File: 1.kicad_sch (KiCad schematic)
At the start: 7 parts, among them Q1 BC107, Q2 BC107, Q3 BC107, Q4 BC107

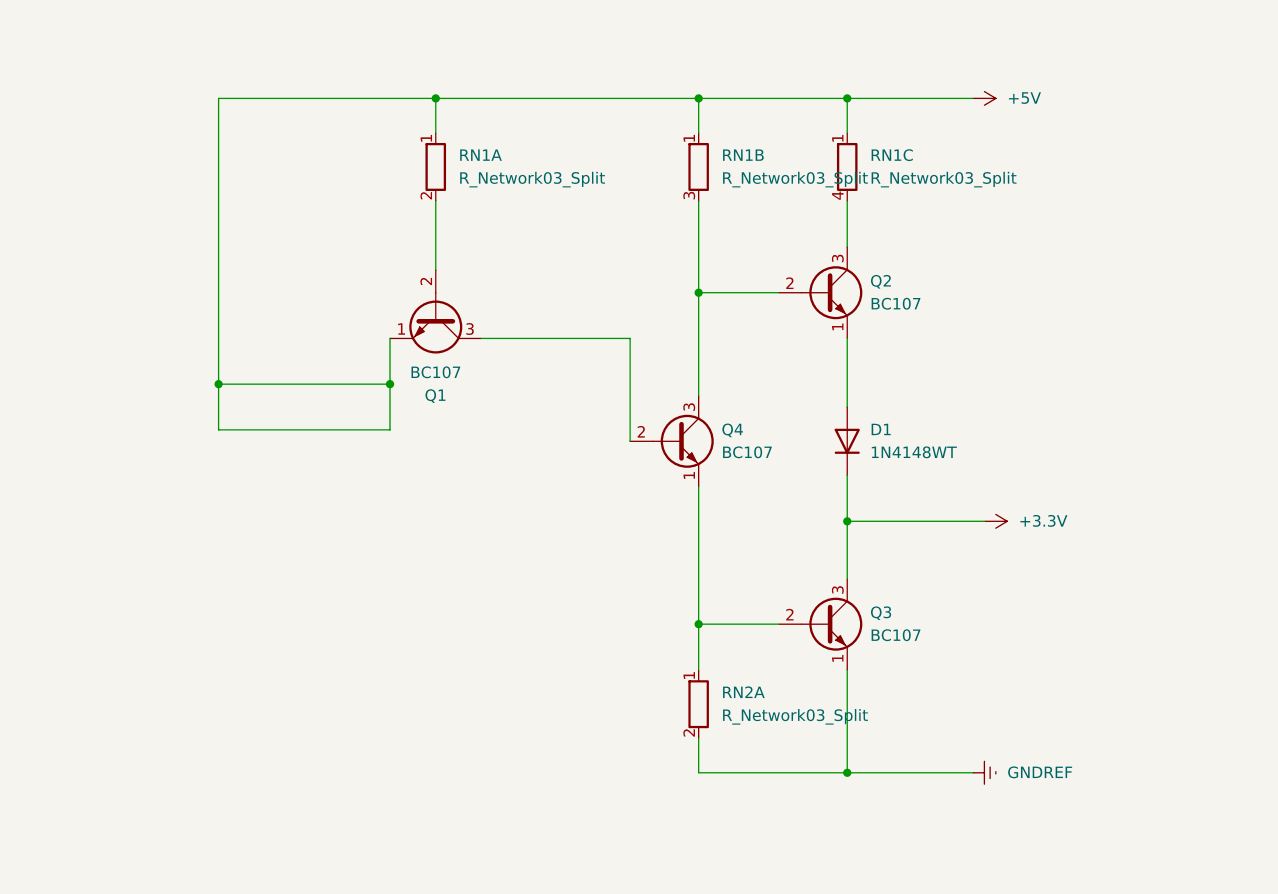
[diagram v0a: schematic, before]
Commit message: 1-create_basic_NAND_logic_discrete_gate: Create correct basic NAND gate schematic.
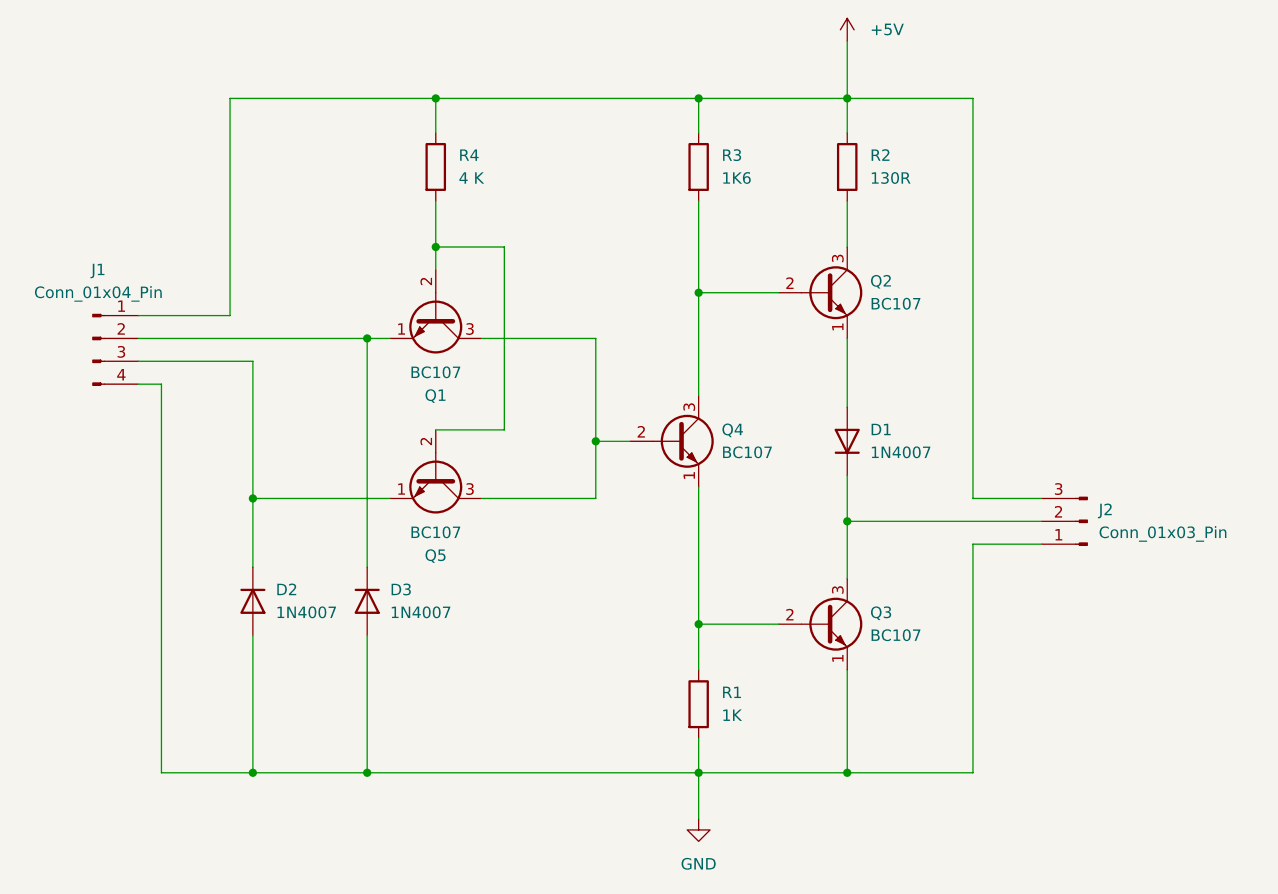
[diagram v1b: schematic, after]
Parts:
- removed D1: 1N4148WT, Diode_SMD:D_SOD-523, symbol Diode:1N4148WT
- removed RN1, RN2: R_Network03_Split, Resistor_THT:R_Array_SIP4, symbol Device:R_Network03_Split
- added D1, D2, D3: 1N4007, Diode_THT:D_DO-41_SOD81_P10.16mm_Horizontal, symbol Diode:1N4007
- added J1: Conn_01x04_Pin, Connector_PinHeader_2.54mm:PinHeader_1x04_P2.54mm_Vertical, symbol Connector:Conn_01x04_Pin
- added J2: Conn_01x03_Pin, Connector_PinHeader_2.54mm:PinHeader_1x03_P2.54mm_Vertical, symbol Connector:Conn_01x03_Pin
- added Q5: BC107, Package_TO_SOT_THT:TO-18-3, symbol Transistor_BJT:BC107
- added R1: 1K, Resistor_THT:R_Axial_DIN0207_L6.3mm_D2.5mm_P10.16mm_Horizontal, symbol Device:R
- added R2: 130R, Resistor_THT:R_Axial_DIN0207_L6.3mm_D2.5mm_P10.16mm_Horizontal, symbol Device:R
- added R3: 1K6, Resistor_THT:R_Axial_DIN0207_L6.3mm_D2.5mm_P10.16mm_Horizontal, symbol Device:R
- added R4: 4 K, Resistor_THT:R_Axial_DIN0207_L6.3mm_D2.5mm_P10.16mm_Horizontal, symbol Device:R
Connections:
- net +5V: now also J1.1 (Pin_1), J2.3 (Pin_3), R2.1, R3.1, R4.1; no longer Q1.1 (E)
- net at Q3.2 (B), Q4.1 (E): now also R1.1
- net at Q2.1 (E): now also D1.2 (A)
- net at Q2.2 (B), Q4.3 (C): now also R3.2
- net at Q2.3 (C): now also R2.2
- net at Q1.2 (B): now also Q5.2 (B), R4.2
- net at Q1.3 (C), Q4.2 (B): now also Q5.3 (C)
- net +3.3V: no longer names the net of Q3.3 (C)
- net +3.3V: now also D1.1 (K), J2.2 (Pin_2)
- net GNDREF renamed GND
- net GND: now also D2.2 (A), D3.2 (A), J1.4 (Pin_4), J2.1 (Pin_1), R1.2
- new net: D3.1 (K), J1.2 (Pin_2), Q1.1 (E)
- new net: D2.1 (K), J1.3 (Pin_3), Q5.1 (E)
